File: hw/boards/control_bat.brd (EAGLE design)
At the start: 101.6 x 30.5 mm, 18 parts, among them U1 579-MCP1703T-3002ECB, U2 771-LPC824M201JDH20J, U3 888-XB24CZ7PIS-004

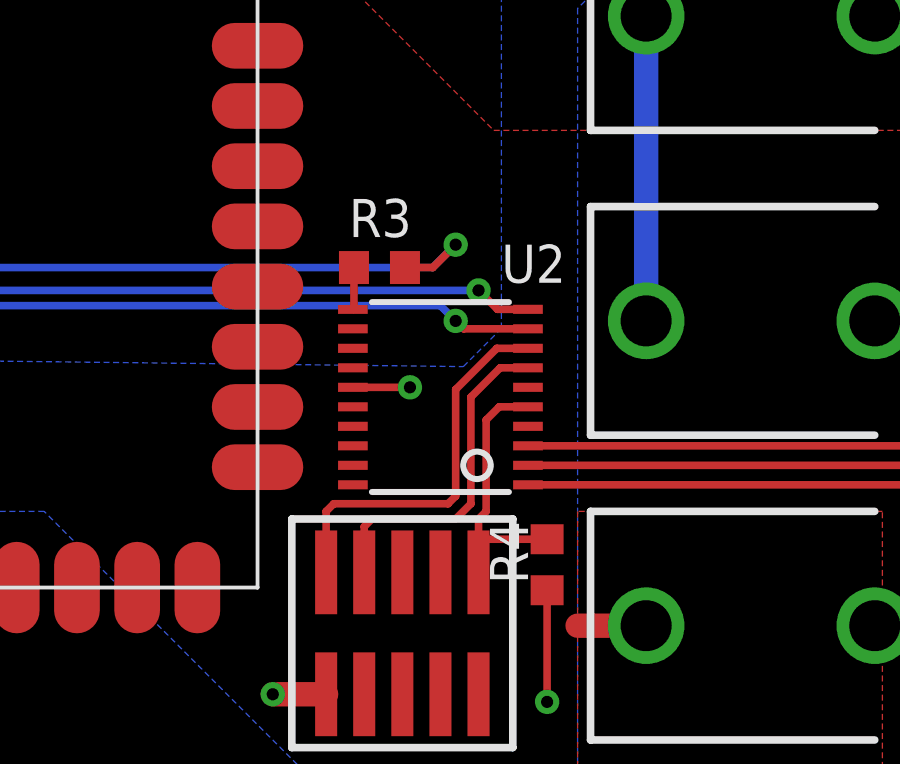
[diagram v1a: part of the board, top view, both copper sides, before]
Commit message: Cleanup some parts, generate BOM.
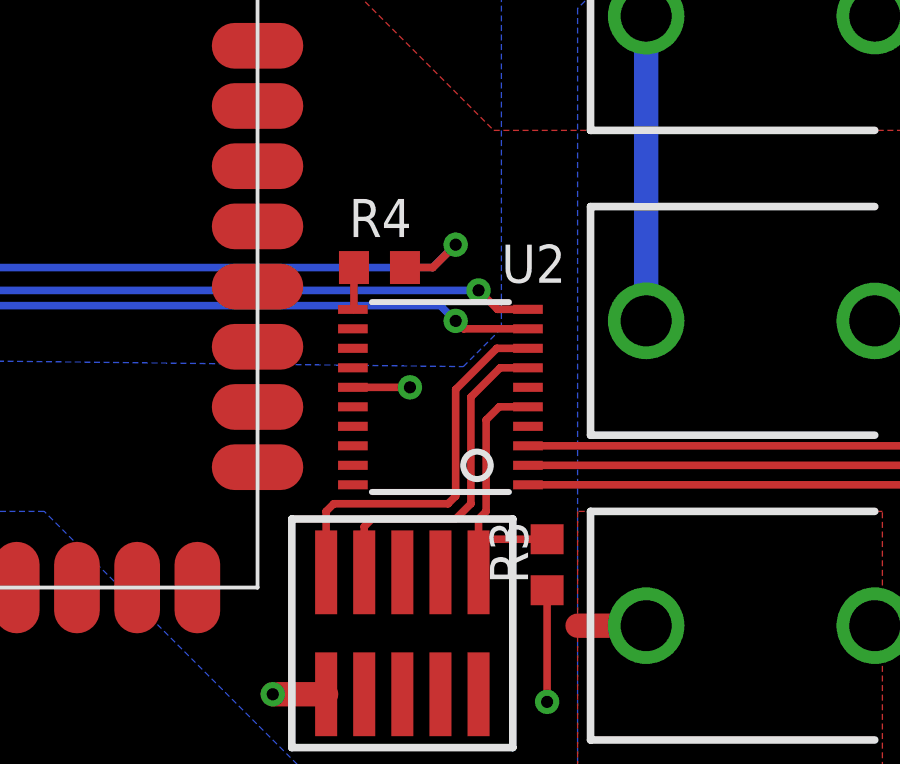
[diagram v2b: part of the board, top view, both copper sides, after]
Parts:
- BAT1, BAT2, BAT3: value (none) -> 534-082
- JP1: value 798-DF132P125V20 -> FTSH-105-01-L; device con-molex:53398-02 -> torpedo:FTSH-105-01-XXX-DV-K
- JP2: value 798-DF134P125V20 -> 798-DF132P125V20; device con-molex:53398-04 -> con-molex:53398-02
- JP3: value FTSH-105-01-L -> 798-DF134P125V20; device torpedo:FTSH-105-01-XXX-DV-K -> con-molex:53398-04
- R3: value 71-CRCW0603220RFKEB -> 71-CRCW0603-10K-E3
- R4: value 71-CRCW0603-10K-E3 -> 71-CRCW0603220RFKEB
- moved JP2 95.3 mm to (4.57, 2.54), turned to 180 degrees
- moved JP3 61.3 mm to (99.1, 15.2), turned to 270 degrees
- moved JP1 34.1 mm to (38.6, 4.83), turned to 0 degrees
- moved R3 11.4 mm to (43.4, 7.11), turned to 90 degrees
- moved R4 11.4 mm to (37.8, 17.0), turned to 0 degrees
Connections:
- net +3V3: now also JP2.1, R3.1; no longer JP3.1, R4.1
- net GND: now also JP1.3, JP1.5, JP1.9, JP3.4; no longer JP2.4, JP3.3, JP3.5, JP3.9
- net IR: now also R4.1; no longer R3.1
- net N$4: now also JP2.2, R4.2; no longer JP1.2, R3.2
- net RST: now also JP1.10, R3.2; no longer JP3.10, R4.2
- net RX: now also JP3.3; no longer JP2.3
- net SWCLK: now also JP1.4; no longer JP3.4
- net SWDIO: now also JP1.2; no longer JP3.2
- net TX: now also JP3.2; no longer JP2.2
- net VIN: now also JP3.1; no longer JP2.1
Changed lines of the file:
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@@
 <attribute name="VALUE" x="95.123" y="23.876" size="0.4064" layer="27" font="vector" rot="R90"/>
 </element>
-<element name="JP2" library="con-molex" package="53398-04" value="798-DF134P125V20" x="99.06" y="15.24" smashed="yes" rot="R270">
+<element name="JP3" library="con-molex" package="53398-04" value="798-DF134P125V20" x="99.06" y="15.24" smashed="yes" rot="R270">
 <attribute name="OC_NEWARK" value="unknown" x="49.53" y="39.37" size="1.778" layer="27" rot="R270" display="off"/>
 <attribute name="MPN" value="" x="49.53" y="39.37" size="1.778" layer="27" rot="R270" display="off"/>
@@
 <attribute name="VALUE" x="95.56" y="18.99" size="1.27" layer="27" rot="R270"/>
 </element>
-<element name="JP3" library="torpedo" package="FTSH-105-01-XXX-DV-K" value="FTSH-105-01-L" x="38.608" y="4.826" smashed="yes"/>
-<element name="BAT3" library="SparkFun-Electromechanical" package="BATTERY-AAA-KIT" value="" x="68.326" y="5.08" smashed="yes" rot="R180">
+<element name="JP1" library="torpedo" package="FTSH-105-01-XXX-DV-K" value="FTSH-105-01-L" x="38.608" y="4.826" smashed="yes"/>
+<element name="BAT3" library="SparkFun-Electromechanical" package="BATTERY-AAA-KIT" value="534-082" x="68.326" y="5.08" smashed="yes" rot="R180">
 <attribute name="PROD_ID" value="BATT-08571" x="68.326" y="5.08" size="1.778" layer="27" rot="R180" display="off"/>
 </element>
 <element name="U3" library="xbee" package="XBEE-SMT" value="888-XB24CZ7PIS-004" x="33.782" y="6.35" smashed="yes" rot="R90"/>
-<element name="BAT2" library="SparkFun-Electromechanical" package="BATTERY-AAA-KIT" value="" x="68.326" y="15.24" smashed="yes">
+<element name="BAT2" library="SparkFun-Electromechanical" package="BATTERY-AAA-KIT" value="534-082" x="68.326" y="15.24" smashed="yes">
 <attribute name="PROD_ID" value="BATT-08571" x="68.326" y="15.24" size="1.778" layer="27" display="off"/>
 </element>
-<element name="BAT1" library="SparkFun-Electromechanical" package="BATTERY-AAA-KIT" value="" x="68.326" y="25.4" smashed="yes" rot="R180">
+<element name="BAT1" library="SparkFun-Electromechanical" package="BATTERY-AAA-KIT" value="534-082" x="68.326" y="25.4" smashed="yes" rot="R180">
 <attribute name="PROD_ID" value="BATT-08571" x="68.326" y="25.4" size="1.778" layer="27" rot="R180" display="off"/>
 </element>
@@
 <attribute name="VALUE" x="10.16" y="-0.635" size="1.27" layer="27"/>
 </element>
-<element name="R3" library="rcl" package="R0603" value="71-CRCW0603220RFKEB" x="37.846" y="17.018" smashed="yes">
+<element name="R4" library="rcl" package="R0603" value="71-CRCW0603220RFKEB" x="37.846" y="17.018" smashed="yes">
 <attribute name="NAME" x="36.83" y="18.034" size="1.27" layer="25"/>
 <attribute name="VALUE" x="37.211" y="15.113" size="1.27" layer="27"/>
@@
 <attribute name="NAME" x="41.91" y="16.51" size="1.27" layer="25" ratio="18"/>
 </element>
-<element name="R4" library="rcl" package="R0603" value="71-CRCW0603-10K-E3" x="43.434" y="7.112" smashed="yes" rot="R90">
+<element name="R3" library="rcl" package="R0603" value="71-CRCW0603-10K-E3" x="43.434" y="7.112" smashed="yes" rot="R90">
 <attribute name="NAME" x="42.799" y="6.477" size="1.27" layer="25" rot="R90"/>
 <attribute name="VALUE" x="45.339" y="6.477" size="1.27" layer="27" rot="R90"/>
 </element>
-<element name="JP1" library="con-molex" package="53398-02" value="798-DF132P125V20" x="4.572" y="2.54" smashed="yes" rot="R180">
+<element name="JP2" library="con-molex" package="53398-02" value="798-DF132P125V20" x="4.572" y="2.54" smashed="yes" rot="R180">
 <attribute name="OC_NEWARK" value="unknown" x="4.572" y="2.54" size="1.778" layer="27" rot="R180" display="off"/>
 <attribute name="MPN" value="" x="4.572" y="2.54" size="1.778" layer="27" rot="R180" display="off"/>
@@
 <contactref element="C1" pad="2"/>
 <contactref element="C2" pad="2"/>
-<contactref element="JP2" pad="4"/>
-<contactref element="JP3" pad="9"/>
-<contactref element="JP3" pad="5"/>
-<contactref element="JP3" pad="3"/>
+<contactref element="JP3" pad="4"/>
+<contactref element="JP1" pad="9"/>
+<contactref element="JP1" pad="5"/>
+<contactref element="JP1" pad="3"/>
 <contactref element="U3" pad="13"/>
 <contactref element="BAT3" pad="GND@1"/>
@@
 <contactref element="U1" pad="2"/>
 <contactref element="C2" pad="1"/>
-<contactref element="JP3" pad="1"/>
+<contactref element="JP1" pad="1"/>
 <contactref element="U3" pad="2"/>
 <contactref element="U3" pad="6"/>
@@
 <wire x1="10.414" y1="10.668" x2="17.272" y2="10.668" width="0.254" layer="1"/>
 <wire x1="17.272" y1="10.668" x2="17.78" y2="10.16" width="0.254" layer="1"/>
-<contactref element="R4" pad="1"/>
+<contactref element="R3" pad="1"/>
 <wire x1="43.434" y1="6.262" x2="43.434" y2="2.54" width="0.254" layer="1"/>
 <via x="43.434" y="2.54" extent="1-16" drill="0.4064"/>
-<contactref element="JP1" pad="1"/>
+<contactref element="JP2" pad="1"/>
 <wire x1="3.947" y1="5.04" x2="3.947" y2="8.519" width="0.254" layer="1"/>
 <wire x1="3.947" y1="8.519" x2="5.334" y2="9.906" width="0.254" layer="1"/>
@@
 <contactref element="U1" pad="3"/>
 <contactref element="C1" pad="1"/>
-<contactref element="JP2" pad="1"/>
+<contactref element="JP3" pad="1"/>
 <contactref element="R1" pad="2"/>
 <contactref element="S1" pad="P$2"/>
@@
 </signal>
 <signal name="TX">
-<contactref element="JP2" pad="2"/>
+<contactref element="JP3" pad="2"/>
 <wire x1="96.56" y1="14.615" x2="94.117" y2="14.615" width="0.254" layer="1"/>
 <wire x1="94.117" y1="14.615" x2="89.927" y2="10.425" width="0.254" layer="1"/>
@@
 </signal>
 <signal name="SWDIO">
-<contactref element="JP3" pad="2"/>
+<contactref element="JP1" pad="2"/>
 <wire x1="40.386" y1="12.954" x2="41.757" y2="14.325" width="0.254" layer="1"/>
 <contactref element="U2" pad="8"/>
@@
 </signal>
 <signal name="SWCLK">
-<contactref element="JP3" pad="4"/>
+<contactref element="JP1" pad="4"/>
 <wire x1="40.894" y1="12.7" x2="41.869" y2="13.675" width="0.254" layer="1"/>
 <contactref element="U2" pad="7"/>
@@
 </signal>
 <signal name="RST">
-<contactref element="JP3" pad="10"/>
+<contactref element="JP1" pad="10"/>
 <wire x1="41.148" y1="6.858" x2="41.148" y2="7.874" width="0.254" layer="1"/>
 <wire x1="41.148" y1="7.962" x2="41.148" y2="8.636" width="0.254" layer="1"/>
@@
 <contactref element="U2" pad="5"/>
 <wire x1="41.839" y1="12.375" x2="42.7958" y2="12.375" width="0.254" layer="1"/>
-<contactref element="R4" pad="2"/>
+<contactref element="R3" pad="2"/>
 <wire x1="43.434" y1="7.962" x2="41.148" y2="7.962" width="0.254" layer="1"/>
 <wire x1="41.148" y1="7.962" x2="41.148" y2="7.874" width="0.254" layer="1"/>
 </signal>
 <signal name="RX">
-<contactref element="JP2" pad="3"/>
+<contactref element="JP3" pad="3"/>
 <wire x1="96.56" y1="15.865" x2="94.605" y2="15.865" width="0.254" layer="1"/>
 <wire x1="94.605" y1="15.865" x2="89.815" y2="11.075" width="0.254" layer="1"/>
@@
 </signal>
 <signal name="N$4">
-<contactref element="R3" pad="2"/>
-<contactref element="JP1" pad="2"/>
+<contactref element="R4" pad="2"/>
+<contactref element="JP2" pad="2"/>
 <wire x1="38.696" y1="17.018" x2="39.624" y2="17.018" width="0.254" layer="1"/>
 <wire x1="39.624" y1="17.018" x2="40.386" y2="17.78" width="0.254" layer="1"/>
@@
 </signal>
 <signal name="IR">
-<contactref element="R3" pad="1"/>
+<contactref element="R4" pad="1"/>
 <contactref element="U2" pad="11"/>
 <wire x1="36.9602" y1="15.625" x2="36.996" y2="15.625" width="0.254" layer="1"/>
